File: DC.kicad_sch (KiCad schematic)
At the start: 84 parts, among them J1 348302001, J2 348302001, J3 757570141, J4 PPTC021LFBN-RC, U6 MCP2551-I-P, U7 NUCLEO-F302R8

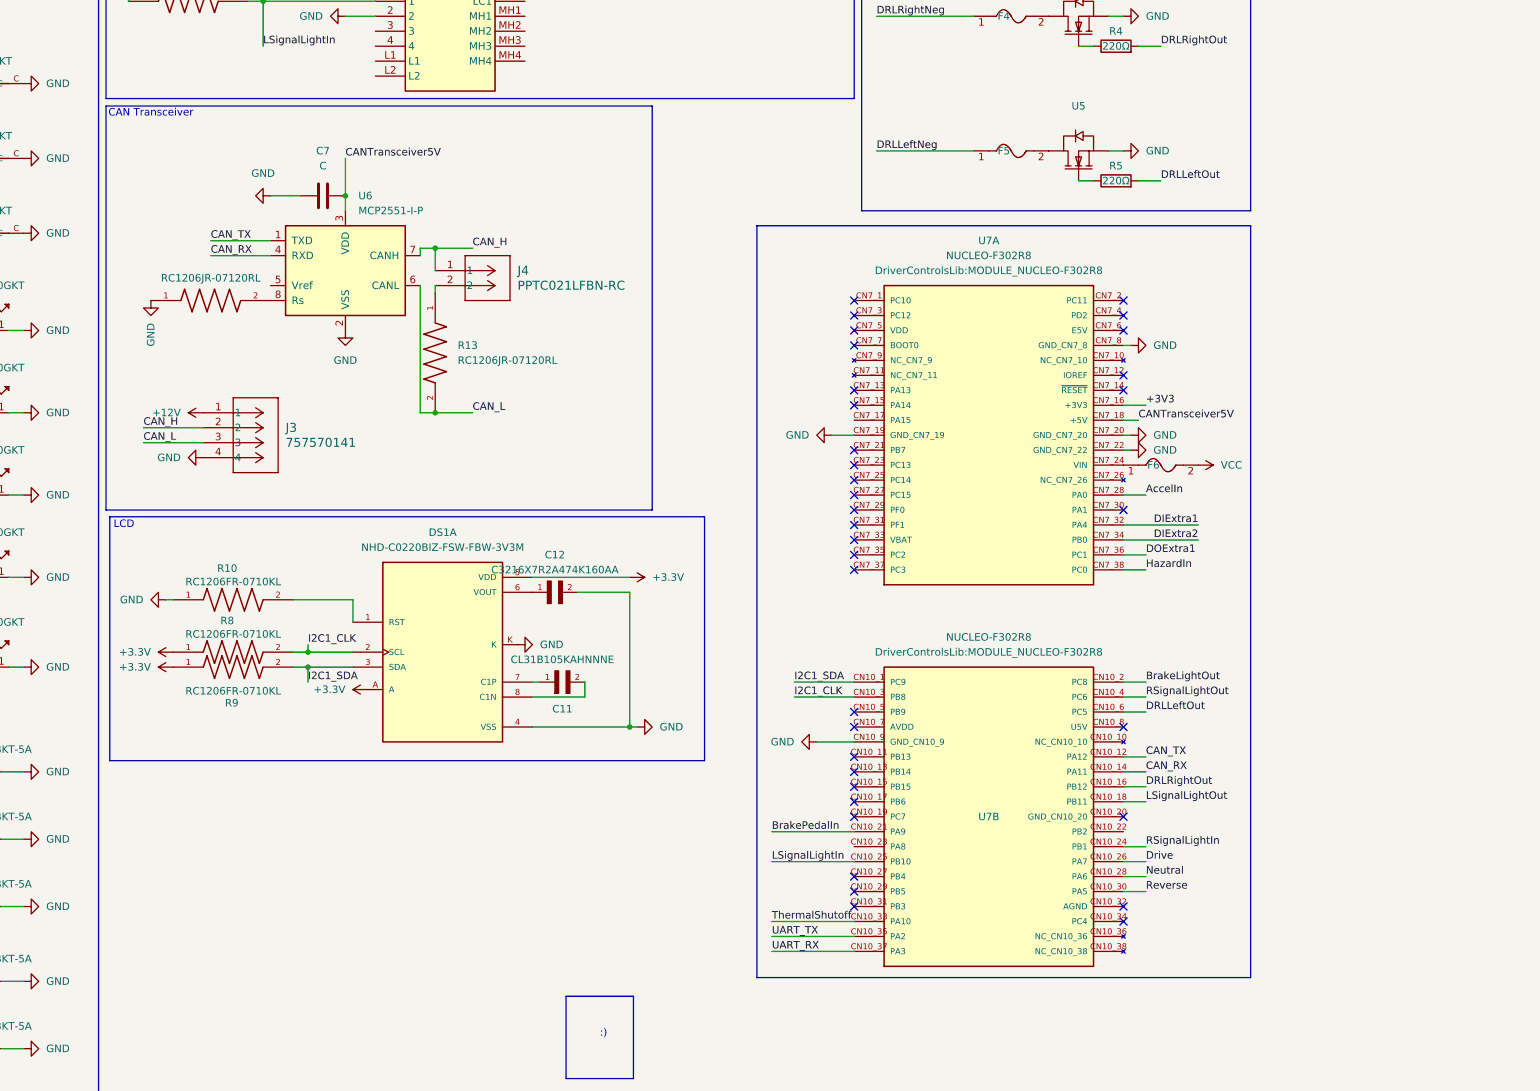
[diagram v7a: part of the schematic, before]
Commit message: Updated symbols/footprints
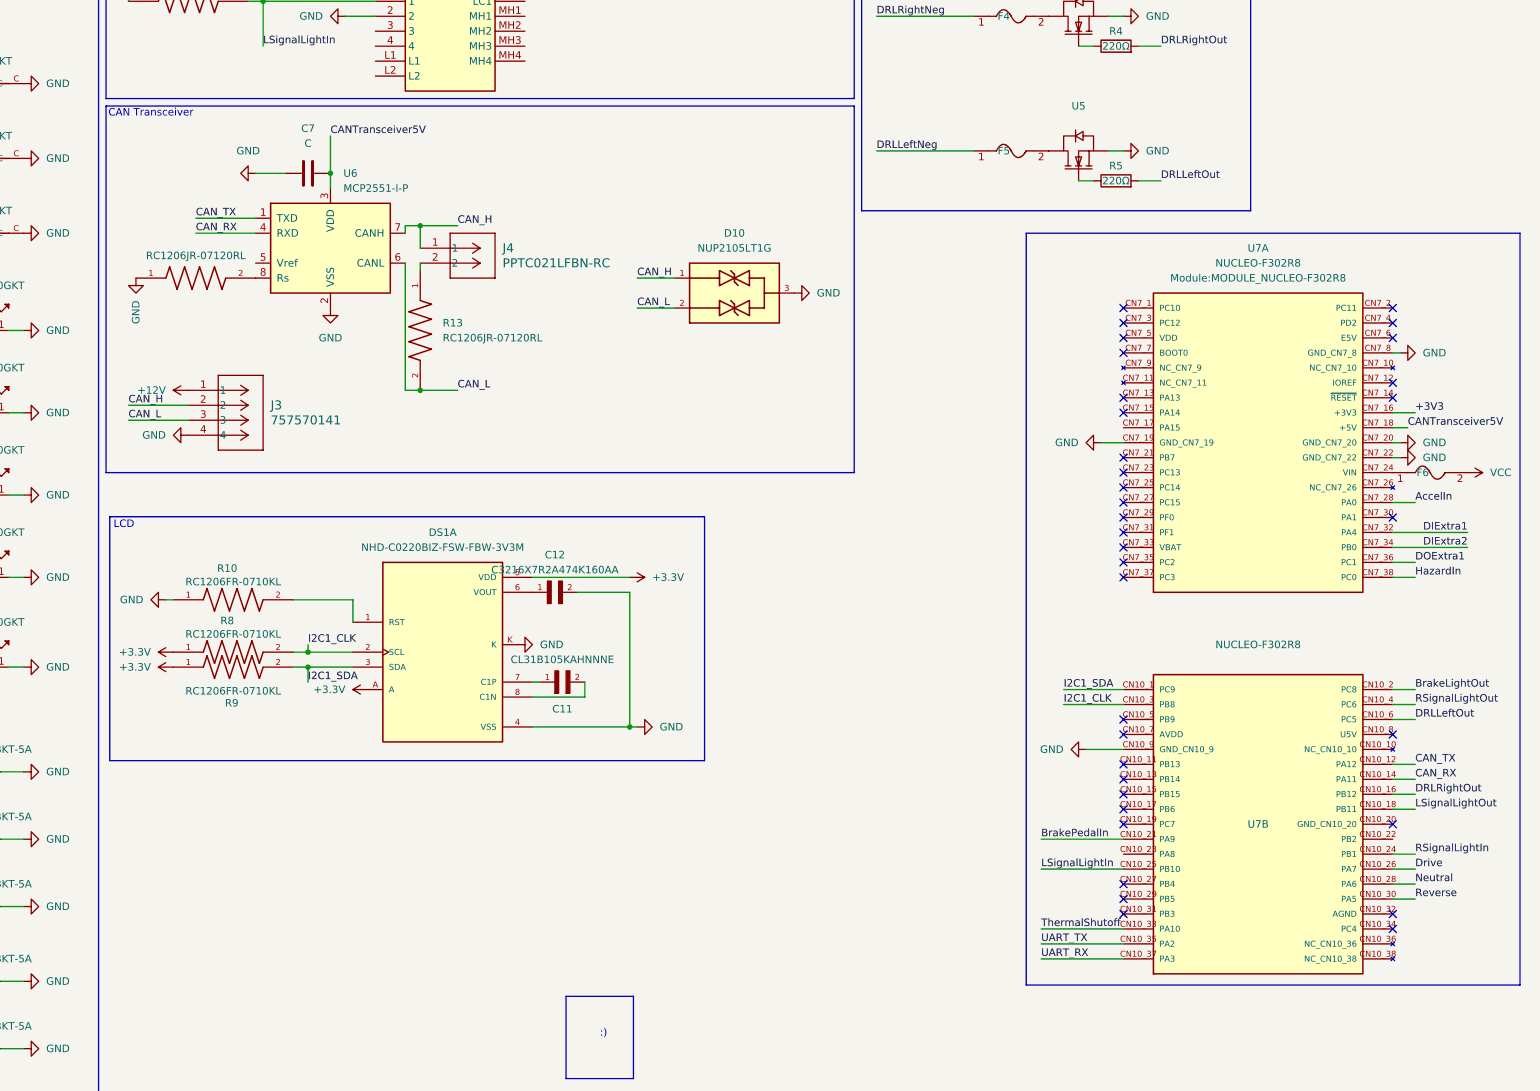
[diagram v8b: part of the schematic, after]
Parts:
- added D10: NUP2105LT1G, Diode_SMD:SOT95P237X111-3N, symbol NUP2105LT1G:NUP2105LT1G
- F4, F5: footprint DriverControlsLib:FUSE-TH_BD5.4-W22.5-P27.5-D0.8 -> Fuse:FUSC3215X66N
- R1, R2, R3, R4, R5: footprint DriverControlsLib:RES-TH_BD2.2-L6.5-P10.50-D0.6 -> Resistor_SMD:RESC3216X70N
- U1, U2, U3, U4, U5: footprint DriverControlsLib:TO220-3_ONS -> Battery:TO254P470X1016X2019-3P
- U7: footprint DriverControlsLib:MODULE_NUCLEO-F302R8 -> Module:MODULE_NUCLEO-F302R8
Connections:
- net CAN_H: now also D10.1
- net CAN_L: now also D10.2
- net GND: now also D10.3
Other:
- moved on the sheet: C7, F6, J3, J4, R13, U6, U7A, U7B
